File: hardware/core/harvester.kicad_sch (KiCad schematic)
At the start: 32 parts, among them U2 BQ25173DSG, U3 BQ25570, U4 SN74LVC1T45

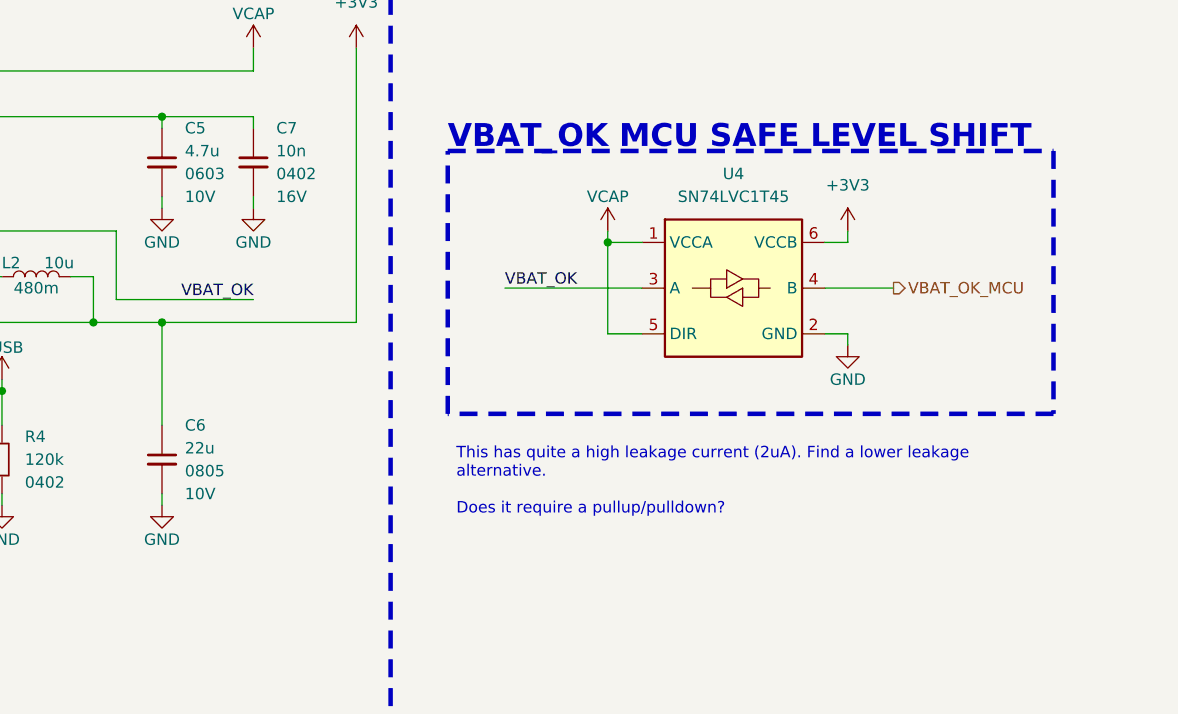
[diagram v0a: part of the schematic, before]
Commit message: updated schematics after some checks to the harvester logic
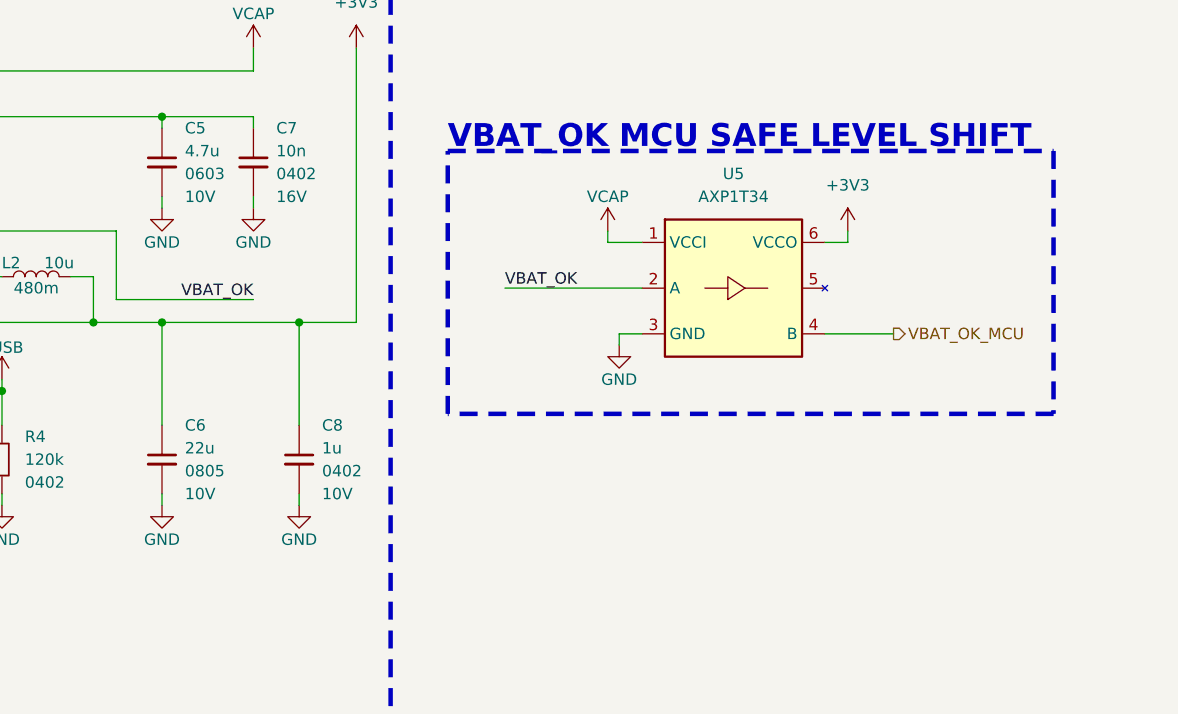
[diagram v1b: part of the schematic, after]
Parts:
- removed U4: SN74LVC1T45, generic:TI_6USON_DPK, symbol ic_logic:SN74LVC1T45DBV
- added C8: 1u, passive:C_0402_1005Metric, symbol passive:C
- added U5: AXP1T34, generic:NX_6SOT1202, symbol ic_logic:AXP1T34GSH
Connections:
- net +3V3: now also C8.1, U5.6 (VCCO)
- net GND: now also C8.2, U5.3 (GND)
- net VBAT_OK: now also U5.2 (A)
- net VBAT_OK_MCU: now also U5.4 (B)
- net VCAP: now also U5.1 (VCCI)
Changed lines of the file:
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@@
 		)
 	)
-	(text_box "This has quite a high leakage current (2uA). Find a lower leakage alternative.\n\nDoes it require a pullup/pulldown?"
-		(exclude_from_sim no)
-		(at 212.09 69.85 0)
-		(size 67.31 11.43)
-		(margins 0.9525 0.9525 0.9525 0.9525)
-		(stroke
-			(width -0.0001)
-			(type solid)
-		)
-		(fill
-			(type color)
-			(color 255 0 0 1)
-		)
-		(effects
-			(font
-				(size 1.27 1.27)
-				(color 255 255 255 1)
-			)
-			(justify left top)
-		)
-	)
 	(text_box "Check MPPT"
 		(exclude_from_sim no)
@@
 	)
 	(junction
-		(at 60.96 72.39)
+		(at 195.58 57.15)
 		(diameter 0)
 		(color 0 0 0 0)
 	)
 	(junction
-		(at 96.52 171.45)
+		(at 60.96 72.39)
 		(diameter 0)
 		(color 0 0 0 0)
 	)
 	(junction
-		(at 229.87 48.26)
+		(at 96.52 171.45)
 		(diameter 0)
 		(color 0 0 0 0)
@@
 	(wire
 		(pts
-			(xy 105.41 39.37) (xy 121.92 39.37)
+			(xy 231.14 58.42) (xy 233.68 58.42)
 		)
 		(stroke
@@
 	(wire
 		(pts
-			(xy 233.68 58.42) (xy 229.87 58.42)
+			(xy 105.41 39.37) (xy 121.92 39.37)
 		)
 		(stroke
@@
 	(wire
 		(pts
+			(xy 195.58 57.15) (xy 201.93 57.15)
+		)
+		(stroke
+			(width 0)
+			(type default)
+		)
+	)
+	(wire
+		(pts
 			(xy 254 48.26) (xy 256.54 48.26)
 		)
@@
 	(wire
 		(pts
-			(xy 254 58.42) (xy 256.54 58.42)
-		)
-		(stroke
-			(width 0)
-			(type default)
-		)
-	)
-	(wire
-		(pts
 			(xy 133.35 181.61) (xy 133.35 189.23)
 		)
@@
 	(wire
 		(pts
-			(xy 261.62 53.34) (xy 254 53.34)
+			(xy 261.62 58.42) (xy 254 58.42)
 		)
 		(stroke
@@
 	(wire
 		(pts
-			(xy 256.54 58.42) (xy 256.54 59.69)
+			(xy 231.14 58.42) (xy 231.14 59.69)
 		)
 		(stroke
@@
 	(wire
 		(pts
-			(xy 229.87 58.42) (xy 229.87 48.26)
+			(xy 195.58 57.15) (xy 195.58 68.58)
 		)
 		(stroke
@@
 	(wire
 		(pts
+			(xy 195.58 76.2) (xy 195.58 77.47)
+		)
+		(stroke
+			(width 0)
+			(type default)
+		)
+	)
+	(wire
+		(pts
 			(xy 96.52 187.96) (xy 96.52 189.23)
 		)
@@
 	(wire
 		(pts
-			(xy 180.34 57.15) (xy 201.93 57.15)
+			(xy 180.34 57.15) (xy 195.58 57.15)
 		)
 		(stroke
@@
 	(hierarchical_label "VBAT_OK_MCU"
 		(shape output)
-		(at 261.62 53.34 0)
+		(at 261.62 58.42 0)
 		(effects
 			(font
@@
 	)
 	(symbol
-		(lib_id "ic_logic:SN74LVC1T45DBV")
-		(at 243.84 53.34 0)
+		(lib_id "passive:C")
+		(at 195.58 68.58 0)
 		(unit 1)
 		(exclude_from_sim no)
@@
 		(dnp no)
 		(fields_autoplaced yes)
-		(property "Reference" "U4"
-			(at 243.84 40.64 0)
+		(property "Reference" "C8"
+			(at 198.12 68.5862 0)
 			(effects
 				(font
 					(size 1.27 1.27)
 				)
+				(justify left)
 			)
 		)
-		(property "Value" "SN74LVC1T45"
-			(at 243.84 43.18 0)
+		(property "Value" "1u"
+			(at 198.12 71.1262 0)
 			(effects
 				(font
 					(size 1.27 1.27)
 				)
+				(justify left)
 			)
 		)
-		(property "Footprint" "generic:TI_6USON_DPK"
-			(at 243.84 64.77 0)
+		(property "Footprint" "passive:C_0402_1005Metric"
+			(at 195.58 68.58 0)
 			(effects
 				(font
@@
 			)
 		)
-		(property "Datasheet" "http://www.ti.com/lit/ds/symlink/sn74lvc1t45.pdf"
-			(at 221.742 74.422 0)
+		(property "Datasheet" ""
+			(at 195.58 68.58 0)
 			(effects
 				(font
@@
 			)
 		)
-		(property "Description" "Single-Bit Dual-Supply Bus Transceiver With Configurable Voltage Translation and 3-State Outputs"
-			(at 242.57 74.168 0)
+		(property "Description" ""
+			(at 195.58 68.58 0)
 			(effects
 				(font
@@
 			)
 		)
-		(property "Sim.Device" ""
-			(at 243.84 53.34 0)
+		(property "Package" "0402"
+			(at 198.12 73.6662 0)
+			(effects
+				(font
+					(size 1.27 1.27)
+				)
+				(justify left)
+			)
+		)
+		(property "Voltage Rating" "10V"
+			(at 198.12 76.2062 0)
+			(effects
+				(font
+					(size 1.27 1.27)
+				)
+				(justify left)
+			)
+		)
+		(property "Part Number" "GRM155Z71A105KE01J"
+			(at 195.58 68.58 0)
 			(effects
 				(font
@@
 			)
 		)
-		(property "Package" "6USON"
-			(at 243.84 53.34 0)
+		(property "Sim.Device" ""
+			(at 195.58 68.58 0)
 			(effects
 				(font
@@
 		(pin "1"
 		)
-		(pin "5"
-		)
-		(pin "6"
-		)
-		(pin "4"
-		)
-		(pin "3"
-		)
 		(pin "2"
 		)
 		(instances
-			(project ""
+			(project "core"
 				(path "/8ec7ca4f-74cd-48e1-b45d-8806dcda5073/cd3a3636-14ab-4325-9b35-d239f2fcdaad"
-					(reference "U4")
+					(reference "C8")
 					(unit 1)
 				)
@@
 	)
 	(symbol
+		(lib_id "ic_logic:AXP1T34GSH")
+		(at 243.84 53.34 0)
+		(unit 1)
+		(exclude_from_sim no)
+		(in_bom yes)
+		(on_board yes)
+		(dnp no)
+		(fields_autoplaced yes)
+		(property "Reference" "U5"
+			(at 243.84 40.64 0)
+			(effects
+				(font
+					(size 1.27 1.27)
+				)
+			)
+		)
+		(property "Value" "AXP1T34"
+			(at 243.84 43.18 0)
+			(effects
+				(font
+					(size 1.27 1.27)
+				)
+			)
+		)
+		(property "Footprint" "generic:NX_6SOT1202"
+			(at 243.84 64.77 0)
+			(effects
+				(font
+					(size 1.27 1.27)
+				)
+				(hide yes)
+			)
+		)
+		(property "Datasheet" "https://assets.nexperia.com/documents/data-sheet/AXP1T34.pdf"
+			(at 221.742 74.422 0)
+			(effects
+				(font
+					(size 1.27 1.27)
+				)
+				(hide yes)
+			)
+		)
+		(property "Description" "Dual supply unidirectional translating buffer"
+			(at 242.57 74.168 0)
+			(effects
+				(font
+					(size 1.27 1.27)
+				)
+				(hide yes)
+			)
+		)
+		(pin "3"
+		)
+		(pin "6"
+		)
+		(pin "4"
+		)
+		(pin "5"
+		)
+		(pin "2"
+		)
+		(pin "1"
+		)
+		(instances
+			(project ""
+				(path "/8ec7ca4f-74cd-48e1-b45d-8806dcda5073/cd3a3636-14ab-4325-9b35-d239f2fcdaad"
+					(reference "U5")
+					(unit 1)
+				)
+			)
+		)
+	)
+	(symbol
 		(lib_id "power_symbol:GND")
 		(at 60.96 97.79 0)
@@
 	(symbol
 		(lib_id "power_symbol:GND")
+		(at 195.58 77.47 0)
+		(unit 1)
+		(exclude_from_sim no)
+		(in_bom yes)
+		(on_board yes)
+		(dnp no)
+		(property "Reference" "#PWR037"
+			(at 195.58 83.82 0)
+			(effects
+				(font
+					(size 1.27 1.27)
+				)
+				(hide yes)
+			)
+		)
+		(property "Value" "GND"
+			(at 195.58 81.28 0)
+			(effects
+				(font
+					(size 1.27 1.27)
+				)
+			)
+		)
+		(property "Footprint" ""
+			(at 195.58 77.47 0)
+			(effects
+				(font
+					(size 1.27 1.27)
+				)
+				(hide yes)
+			)
+		)
+		(property "Datasheet" ""
+			(at 195.58 77.47 0)
+			(effects
+				(font
+					(size 1.27 1.27)
+				)
+				(hide yes)
+			)
+		)
+		(property "Description" "Power symbol creates a global label with name \"GND\" , ground"
+			(at 195.58 77.47 0)
+			(effects
+				(font
+					(size 1.27 1.27)
+				)
+				(hide yes)
+			)
+		)
+		(pin "1"
+		)
+		(instances
+			(project "core"
+				(path "/8ec7ca4f-74cd-48e1-b45d-8806dcda5073/cd3a3636-14ab-4325-9b35-d239f2fcdaad"
+					(reference "#PWR037")
+					(unit 1)
+				)
+			)
+		)
+	)
+	(symbol
+		(lib_id "power_symbol:GND")
 		(at 96.52 189.23 0)
 		(unit 1)
@@
 	(symbol
 		(lib_id "power_symbol:GND")
-		(at 256.54 59.69 0)
+		(at 231.14 59.69 0)
 		(unit 1)
 		(exclude_from_sim no)
@@
 		(dnp no)
 		(property "Reference" "#PWR036"
-			(at 256.54 66.04 0)
+			(at 231.14 66.04 0)
 			(effects
 				(font
@@
 		)
 		(property "Value" "GND"
-			(at 256.54 63.5 0)
+			(at 231.14 63.5 0)
 			(effects
 				(font
@@
 		)
 		(property "Footprint" ""
-			(at 256.54 59.69 0)
+			(at 231.14 59.69 0)
 			(effects
 				(font
@@
 		)
 		(property "Datasheet" ""
-			(at 256.54 59.69 0)
+			(at 231.14 59.69 0)
 			(effects
 				(font
@@
 		)
 		(property "Description" "Power symbol creates a global label with name \"GND\" , ground"
-			(at 256.54 59.69 0)
+			(at 231.14 59.69 0)
 			(effects
 				(font

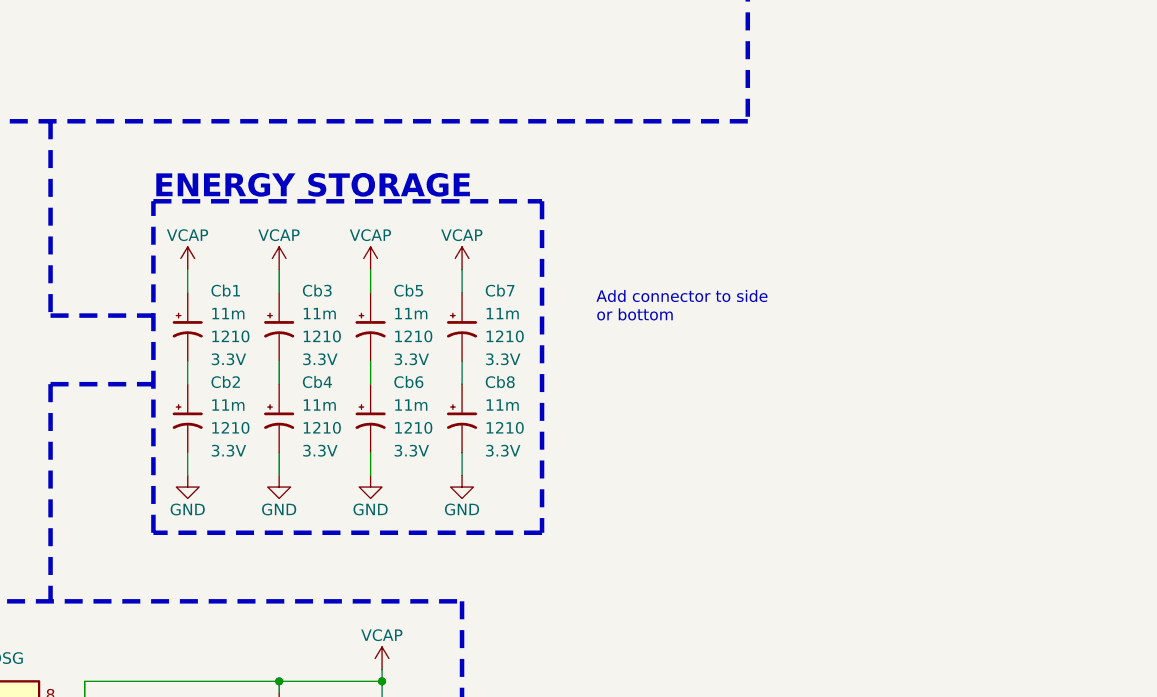
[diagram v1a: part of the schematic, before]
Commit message: Updated with cap and connector
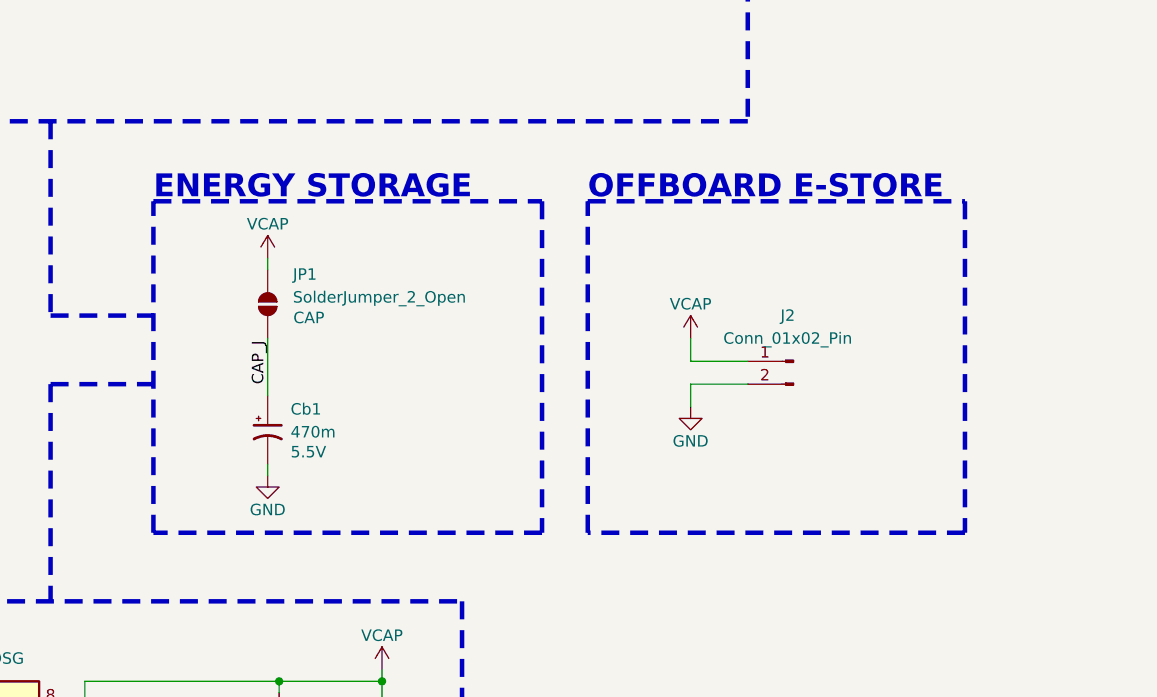
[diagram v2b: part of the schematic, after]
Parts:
- removed Cb2, Cb3, Cb4, Cb5, Cb6, Cb7, Cb8: 11m, part_specific:SEIKO_CPH3225A, symbol passive:C_polarised
- added J2: Conn_01x02_Pin, connectors:PinHeader_1x02_P2.54mm_Horizontal, symbol connectors:Conn_01x02_Pin
- added JP1: SolderJumper_2_Open, misc:SolderJumper2_Open_0402, symbol misc:SolderJumper_2_Open
- Cb1: value 11m -> 470m; footprint part_specific:SEIKO_CPH3225A -> part_specific:EATON_KR5R5H474R; Package 1210 -> (none); Part Number CPH3225A -> KR-5R5H474-R; Voltage Rating 3.3V -> 5.5V
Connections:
- net GND: now also Cb1.2, J2.2 (Pin_2)
- net VCAP: now also J2.1 (Pin_1), JP1.2 (B); no longer Cb1.1
- new net CAP_J: Cb1.1, JP1.1 (A)
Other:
- note added: "OFFBOARD E-STORE"
- moved on the sheet: Cb1

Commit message: updated layout with footprint changes
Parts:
- SC1: Part Number (none) -> KXOB25-14X1TF-TR
- U2: Part Number (none) -> BQ25173DSGR
- U3: Part Number (none) -> BQ25570RGRR
- U5: Part Number (none) -> 74AXP1T34GSH
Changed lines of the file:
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@@
 			)
 		)
+		(property "Part Number" "KXOB25-14X1TF-TR"
+			(at 30.48 68.58 0)
+			(effects
+				(font
+					(size 1.27 1.27)
+				)
+				(hide yes)
+			)
+		)
 		(pin "1"
 		)
@@
 			)
 		)
+		(property "Part Number" "BQ25173DSGR"
+			(at 119.38 176.53 0)
+			(effects
+				(font
+					(size 1.27 1.27)
+				)
+				(hide yes)
+			)
+		)
 		(pin "9"
 		)
@@
 			)
 		)
+		(property "Part Number" "74AXP1T34GSH"
+			(at 243.84 53.34 0)
+			(effects
+				(font
+					(size 1.27 1.27)
+				)
+				(hide yes)
+			)
+		)
 		(pin "3"
 		)
@@
 			(at 137.16 41.91 0)
 			(effects
+				(font
+					(size 1.27 1.27)
+				)
+				(hide yes)
+			)
+		)
+		(property "Part Number" "BQ25570RGRR"
+			(at 137.16 41.91 0)
+			(effects

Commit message: added variables
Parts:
- J2: now not fitted
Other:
- title: (none) -> Xihe
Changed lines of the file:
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@@
 	(generator_version "9.0")
 	(paper "A4")
+	(title_block
+		(title "Xihe")
+		(date "2025-08-19")
+		(rev "0.1")
+	)
 	(rectangle
 		(start 139.7 115.57)
@@
 		(in_bom yes)
 		(on_board yes)
-		(dnp no)
+		(dnp yes)
 		(property "Reference" "J2"
 			(at 210.185 128.27 0)

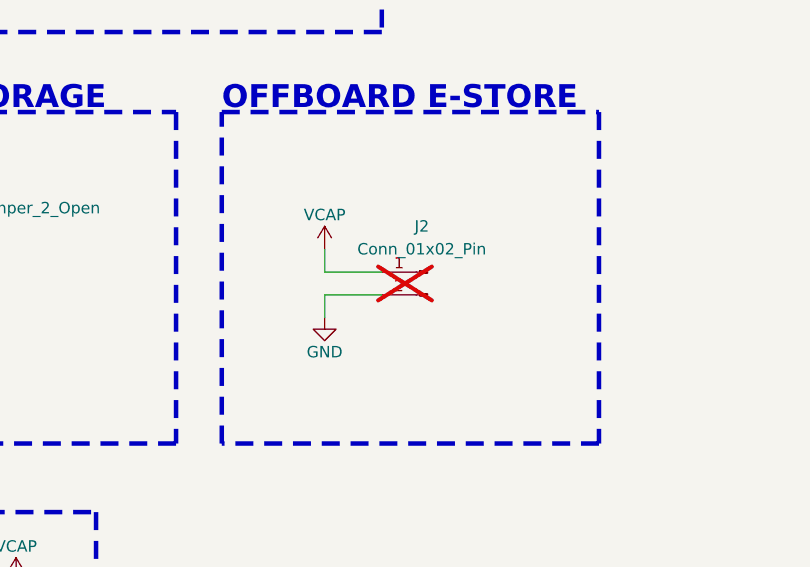
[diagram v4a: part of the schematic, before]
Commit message: Minor part choice changes and appropriate board updates
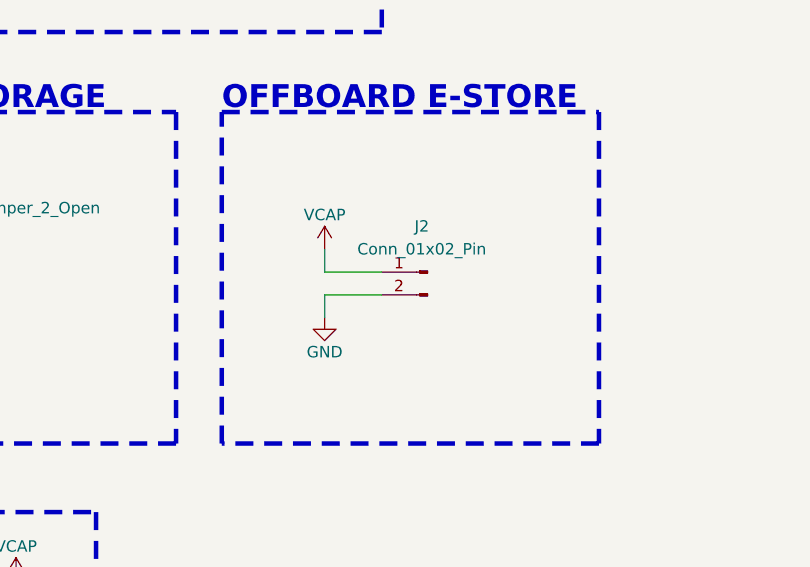
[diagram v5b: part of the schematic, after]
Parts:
- Cb1: Part Number KR-5R5H474-R -> EDC474Z5R5H
- J2: footprint connectors:PinHeader_1x02_P2.54mm_Horizontal -> connectors:PD_801-83-002-20-001101; Part Number SSA-102-W-T-RA -> 801-83-002-20-001101; now fitted
- SC1: Part Number KXOB25-14X1TF-TR -> KXOB25-03X4F-TR
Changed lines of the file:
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@@
 	)
 	(symbol
+		(lib_id "power_symbol:VUSB")
+		(at 162.56 63.5 0)
+		(unit 1)
+		(exclude_from_sim no)
+		(in_bom yes)
+		(on_board yes)
+		(dnp no)
+		(property "Reference" "#PWR021"
+			(at 162.56 67.31 0)
+			(effects
+				(font
+					(size 1.27 1.27)
+				)
+				(hide yes)
+			)
+		)
+		(property "Value" "VUSB"
+			(at 162.56 59.944 0)
+			(effects
+				(font
+					(size 1.27 1.27)
+				)
+			)
+		)
+		(property "Footprint" ""
+			(at 162.56 63.5 0)
+			(effects
+				(font
+					(size 1.27 1.27)
+				)
+				(hide yes)
+			)
+		)
+		(property "Datasheet" ""
+			(at 162.56 63.5 0)
+			(effects
+				(font
+					(size 1.27 1.27)
+				)
+				(hide yes)
+			)
+		)
+		(property "Description" "Power symbol creates a global label with name \"VUSB\""
+			(at 162.56 63.5 0)
+			(effects
+				(font
+					(size 1.27 1.27)
+				)
+				(hide yes)
+			)
+		)
+		(pin "1"
+		)
+		(instances
+			(project "core"
+				(path "/8ec7ca4f-74cd-48e1-b45d-8806dcda5073/cd3a3636-14ab-4325-9b35-d239f2fcdaad"
+					(reference "#PWR021")
+					(unit 1)
+				)
+			)
+		)
+	)
+	(symbol
 		(lib_id "passive:R")
 		(at 91.44 62.23 0)
@@
 			)
 		)
-		(property "Part Number" "KR-5R5H474-R"
+		(property "Part Number" "EDC474Z5R5H"
 			(at 152.4 137.16 0)
 			(effects
@@
 			)
 		)
-		(property "Part Number" "KXOB25-14X1TF-TR"
+		(property "Part Number" "KXOB25-03X4F-TR"
 			(at 30.48 68.58 0)
 			(effects
@@
 		(in_bom yes)
 		(on_board yes)
-		(dnp yes)
+		(dnp no)
 		(property "Reference" "J2"
 			(at 210.185 128.27 0)
@@
 			)
 		)
-		(property "Footprint" "connectors:PinHeader_1x02_P2.54mm_Horizontal"
+		(property "Footprint" "connectors:PD_801-83-002-20-001101"
 			(at 210.82 135.89 0)
 			(effects
@@
 			)
 		)
-		(property "Part Number" "SSA-102-W-T-RA"
+		(property "Part Number" "801-83-002-20-001101"
 			(at 210.82 135.89 0)
 			(effects
@@
 					(unit 1)
 				)
-			)
-		)
-	)
-	(symbol
-		(lib_id "bpower:VUSB")
-		(at 162.56 63.5 0)
-		(unit 1)
-		(exclude_from_sim no)
-		(in_bom yes)
-		(on_board yes)
-		(dnp no)
-		(property "Reference" "#PWR021"
-			(at 162.56 67.31 0)
-			(effects
-				(font
-					(size 1.27 1.27)
-				)
-				(hide yes)
-			)
-		)
-		(property "Value" "VUSB"
-			(at 162.56 59.944 0)
-			(effects
-				(font
-					(size 1.27 1.27)
-				)
-			)
-		)
-		(property "Footprint" ""
-			(at 162.56 63.5 0)
-			(effects
-				(font
-					(size 1.27 1.27)
-				)
-				(hide yes)
-			)
-		)
-		(property "Datasheet" ""
-			(at 162.56 63.5 0)
-			(effects
-				(font
-					(size 1.27 1.27)
-				)
-				(hide yes)
-			)
-		)
-		(property "Description" "Power symbol creates a global label with name \"VUSB\""
-			(at 162.56 63.5 0)
-			(effects
-				(font
-					(size 1.27 1.27)
-				)
-				(hide yes)
-			)
-		)
-		(pin "1"
-		)
-		(instances
-			(project "core"
-				(path "/8ec7ca4f-74cd-48e1-b45d-8806dcda5073/cd3a3636-14ab-4325-9b35-d239f2fcdaad"
-					(reference "#PWR021")
-					(unit 1)
-				)

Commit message: bom updates
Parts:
- C1, C2, C3, C4, C5, C6, C7, C8, L2: Manufacturer (none) -> Murata Electronics; Mounting Type (none) -> smt
- Cb1: Manufacturer (none) -> Cornell Dubilier Knowles; Mounting Type (none) -> tht
- J2: Manufacturer (none) -> Preci-Dip; Mounting Type (none) -> tht
- JP1: Mounting Type (none) -> smt
- L1: Manufacturer (none) -> Taiyo Yuden; Mounting Type (none) -> smt
- R1, R2, R3, R4, ROK1, ROK2, ROK3, ROUT1, ROUT2, ROV1, ROV2: Manufacturer (none) -> YAGEO; Mounting Type (none) -> smt
- SC1: Manufacturer (none) -> ANYSOLAR Ltd; Mounting Type (none) -> smt
- U2: Manufacturer (none) -> Texas Instruments; Mounting Type (none) -> smt
- U3: Manufacturer (none) -> Texas Instruments; Mounting Type (none) -> smt; Package 20QFN -> 20VQFN
- U5: Manufacturer (none) -> Nexperia USA Inc.; Mounting Type (none) -> smt; Package (none) -> 6XSON
